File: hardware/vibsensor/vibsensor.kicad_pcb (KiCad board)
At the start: 4 copper layers, 26 x 26 mm, 50 parts, among them J1 M8 LEADS, J2 SWD, U1 STM32G473CEU6, U2 TPS560430XDBVR, U3 TLV75533PDBVR, U4 IIS3DWBTR, U5 TMP117AIDRVR, U6 TCAN1044VDR, Y1 8MHz

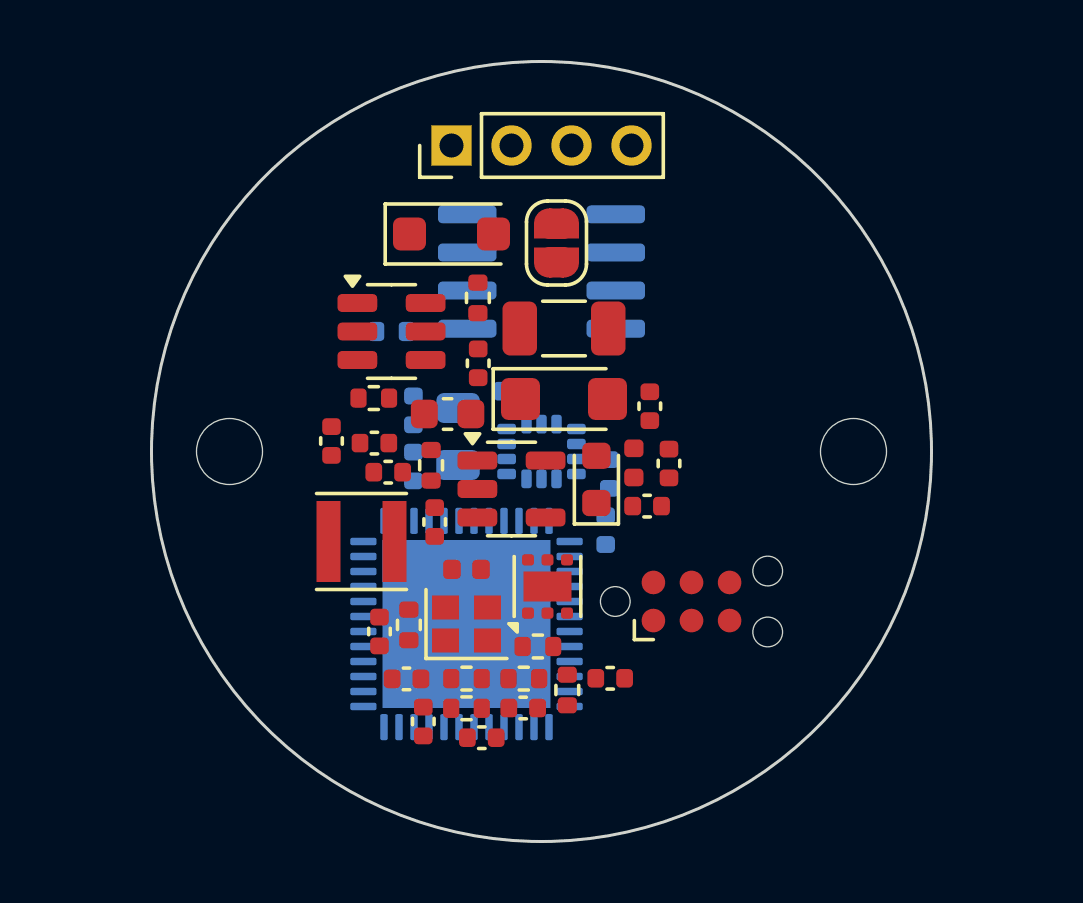
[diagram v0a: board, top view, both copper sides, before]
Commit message: vibsensor: enclosure concept "Shard"; the board shaped to it
- hardware/vibsensor/enclosure: parametric OpenSCAD model: milled
  aluminium base with a solid floor, two swept-back M4 lugs (or an M6
  stud under the accelerometer), the board on two bosses, potted cavity,
  faceted cover with a light-pipe slit and +X arrow on the ridge, M8
  socket in the tail tilted 15 deg; STLs, renders, README with open points
- the board: 32 x 18 mm, chamfered to the same shape (nose = +X), M2
  holes at +-9 mm, MCU on top at the centre over the IIS3DWB; placed,
  DRC clean but for unrouted connections
- kigen: polygon board outlines; silkscreen overlaps (warnings) allowed

Co-Authored-By: Claude Opus 5.5 <noreply@anthropic.com>
Claude-Session: https://claude.ai/code/session_015Arx3mBYT6sxmWehm9yoEa
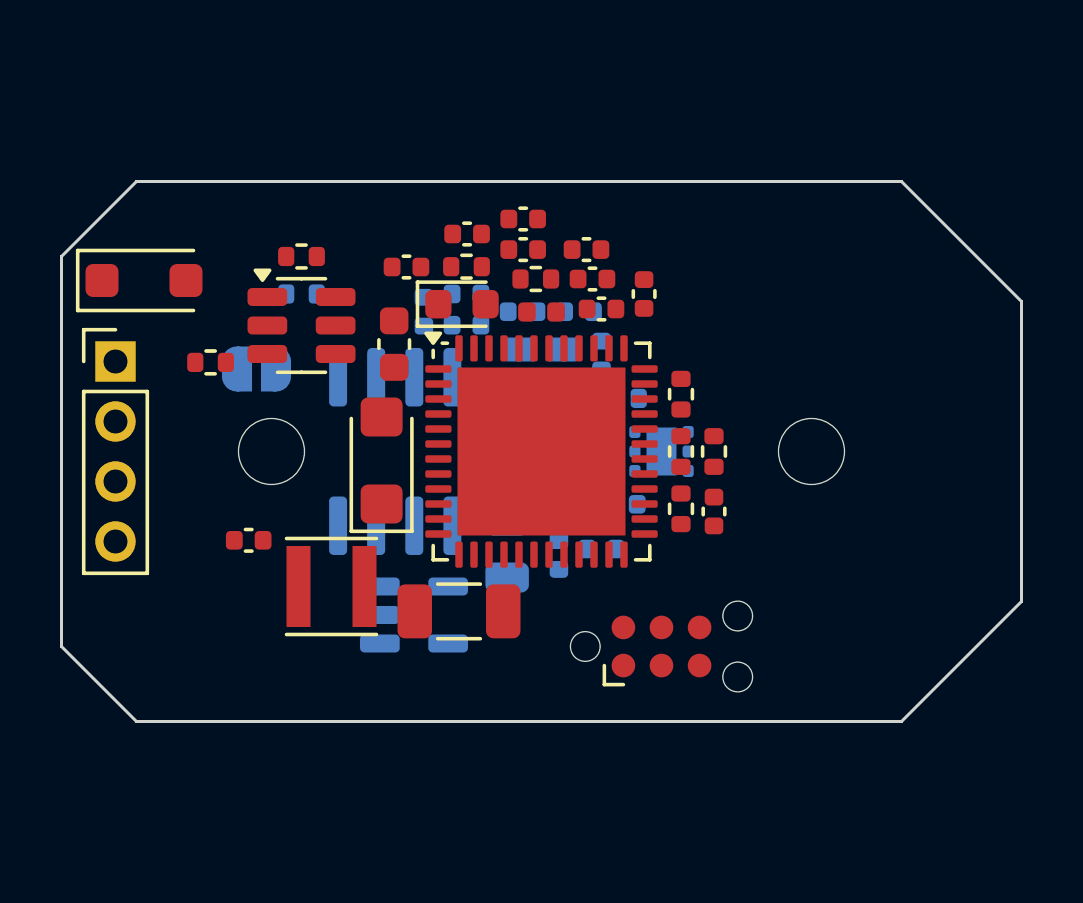
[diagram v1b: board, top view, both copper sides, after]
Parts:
- C12, C13, C14, C17, C19, C7, C8, FB1, JP1, R2, R9, U3, U5, Y1: moved to B.Cu
- C18, C20, C21, R1, U1: moved to F.Cu
- moved C10 13.9 mm to (102.0, 95.2)
- moved C11 13.7 mm to (101.7, 94.2), turned to 0 degrees
- moved J1 13.3 mm to (85.8, 97.0), turned to 0 degrees
- moved R6 12.3 mm to (99.8, 94.2)
- moved C9 12.0 mm to (105.8, 102.0)
- moved R8 11.7 mm to (105.8, 100.0)
- moved JP1 10.8 mm to (90.5, 97.2), turned to 0 degrees
- moved R7 10.8 mm to (104.7, 98.1), turned to 90 degrees
- moved R3 10.4 mm to (104.7, 100.0), turned to 90 degrees
- moved D1 10.4 mm to (86.8, 94.3)
- moved C1 10.1 mm to (97.2, 105.3)
- moved R9 9.90 mm to (102.7, 98.2), turned to 0 degrees
- moved R4 9.76 mm to (104.7, 101.9), turned to 90 degrees
- moved C20 9.25 mm to (101.5, 93.3), turned to 0 degrees
- moved R10 9.17 mm to (89.0, 97.0), turned to 0 degrees
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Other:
- board size 26 x 26 mm -> 32 x 18 mm

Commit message: vibsensor: two M8 sockets (IN / OUT) and a terminator plug
The sensors daisy-chain on standard M8 4-pin cables: IN (male) and OUT
(female), wired 1:1 on the board (J1, J3), so supply and CAN pass
through. The on-board termination (JP1, R10) is gone; the last sensor's
OUT takes an M8 male plug with the 120 ohm inside.

Enclosure: both sockets on the tail's 45-degree faces, the M4 lugs on
the X axis at the nose and tail, a terminated render. Docs updated.

Co-Authored-By: Claude Opus 5.5 <noreply@anthropic.com>
Claude-Session: https://claude.ai/code/session_015Arx3mBYT6sxmWehm9yoEa
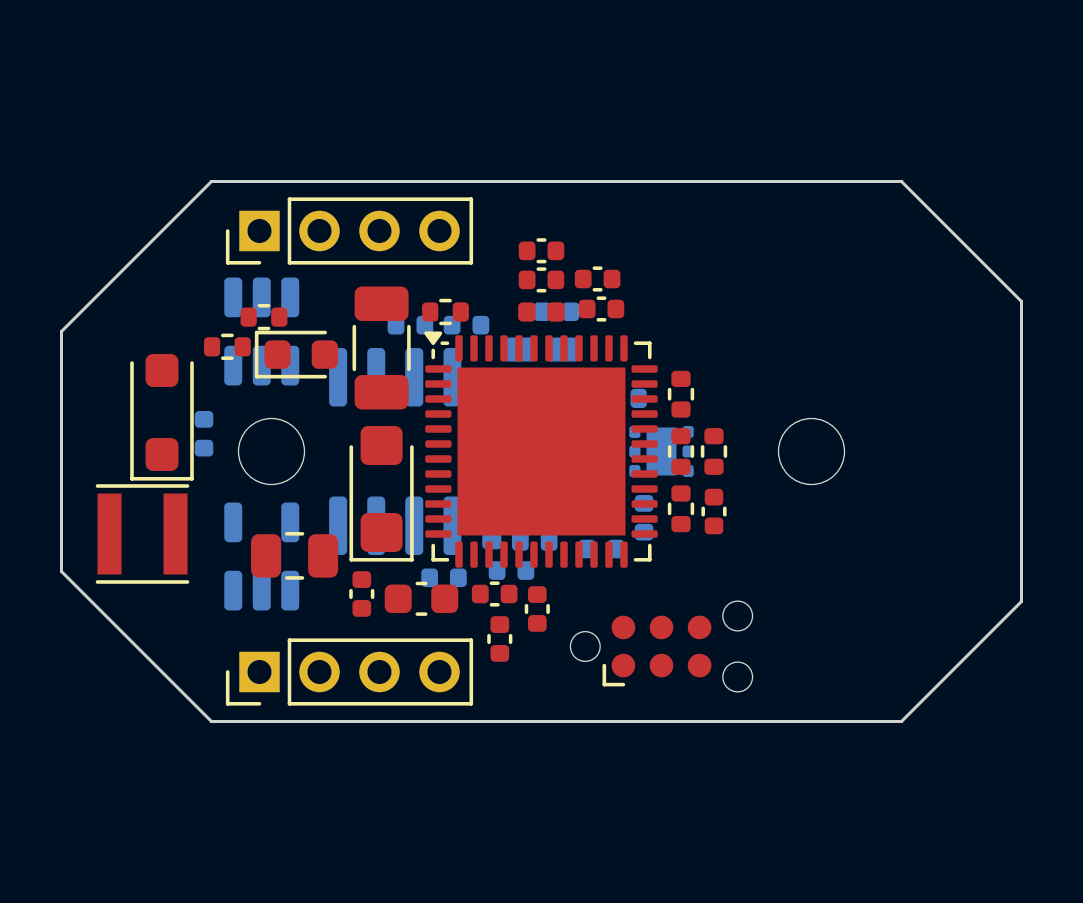
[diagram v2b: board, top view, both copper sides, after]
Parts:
- removed JP1: TERM, Jumper:SolderJumper-2_P1.3mm_Open_RoundedPad1.0x1.5mm
- removed R10: 120, Resistor_SMD:R_0402_1005Metric
- added J3: M8 OUT, Connector_PinHeader_2.00mm:PinHeader_1x04_P2.00mm_Vertical, F.Cu at (90.6, 107.3)
- C13, C17, C19, C4, R2: moved to F.Cu
- C18, C20, C21, C3, R5, U2: moved to B.Cu
- J1: value M8 LEADS -> M8 IN
- moved C6 14.0 mm to (98.6, 106.2), turned to 90 degrees
- moved C15 12.0 mm to (99.9, 105.2), turned to 90 degrees
- moved C2 11.0 mm to (94.0, 104.8), turned to 90 degrees
- moved C22 9.34 mm to (99.0, 104.0)
- moved C1 9.15 mm to (94.7, 96.5), turned to 90 degrees
- moved C13 9.01 mm to (98.4, 104.8)
- moved C5 8.90 mm to (96.8, 104.2), turned to 0 degrees
- moved R5 8.68 mm to (98.3, 102.5), turned to 90 degrees
- moved C16 8.54 mm to (96.0, 104.9), turned to 0 degrees
- moved C14 7.67 mm to (99.8, 103.0)
- moved C4 7.09 mm to (91.8, 103.5), turned to 0 degrees
- moved L1 6.54 mm to (86.7, 102.8)
- moved J1 6.48 mm to (90.6, 92.7), turned to 90 degrees
- moved D3 5.62 mm to (92.0, 96.8)
- moved U3 5.44 mm to (90.7, 103.5), turned to 90 degrees
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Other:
- outline, holes or cut-outs redrawn
